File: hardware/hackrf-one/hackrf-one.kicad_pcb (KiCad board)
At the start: 4 copper layers, 120 x 75 mm, 444 parts, among them J1 USB-MICRO-B, J10 GND_CLIP, J2 RF-SHIELD-FRAME, J3 RF-SHIELD-COVER, J4 MOUNTING_HOLE, J5 MOUNTING_HOLE, J6 MOUNTING_HOLE, J7 MOUNTING_HOLE, J8 MOUNTING_HOLE, J9 MOUNTING_HOLE, P1 1V8, P13 GPO1, P14 XCVR_CLKOUT, P15 INTR, P16 CLKIN, P17 GPO6, P18 OEB, P19 GPO3, P2 CLKOUT, P20 GPIO, P21 REF_IN, P22 I2S, P23 DBGEN, P24 TRST, P25 LPC_ISP, P26 LPC_JTAG, P27 MIXER_SDATA, P28 SD, P29 CPLD_JTAG, P3 GND, P30 BANK2_AUX, P31 MIXER_SCLK, P32 MIXER_ENX, P33 MIXER_RESETX, P34 MIX_BYPASS, P35 !MIX_BYPASS, P36 VAA, P37 SCL, P38 SDA, P39 SSP1_SCK, P4 ANTENNA, P40 SSP1_MOSI, P41 SSP1_MISO, P42 TX, P43 RX, P44 HP, P45 LP, P46 TX_MIX_BP, P47 RX_MIX_BP, P48 TX_AMP, P49 RX_AMP, P5 LEDS, P50 AMP_BYPASS, P51 !TX_AMP_PWR, P52 !RX_AMP_PWR, P53 CS_XCVR, P54 CS_AD, P55 TXENABLE, P56 RXENABLE, P57 XTAL2, P58 GCK1, P59 GCK2, P6 GPO4, P60 SGPIO_CLK, P61 DA0, P62 DA7, P63 DD0, P64 DD9, P65 DA4, P66 DD5, P67 RSSI, P68 SPIFI_CS, P69 VREGMODE, P7 GPO2, P70 EN_1V8, P71 ID, P72 GP_CLKIN, P73 P1_2, P74 P1_1, P75 GP_CLKIN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

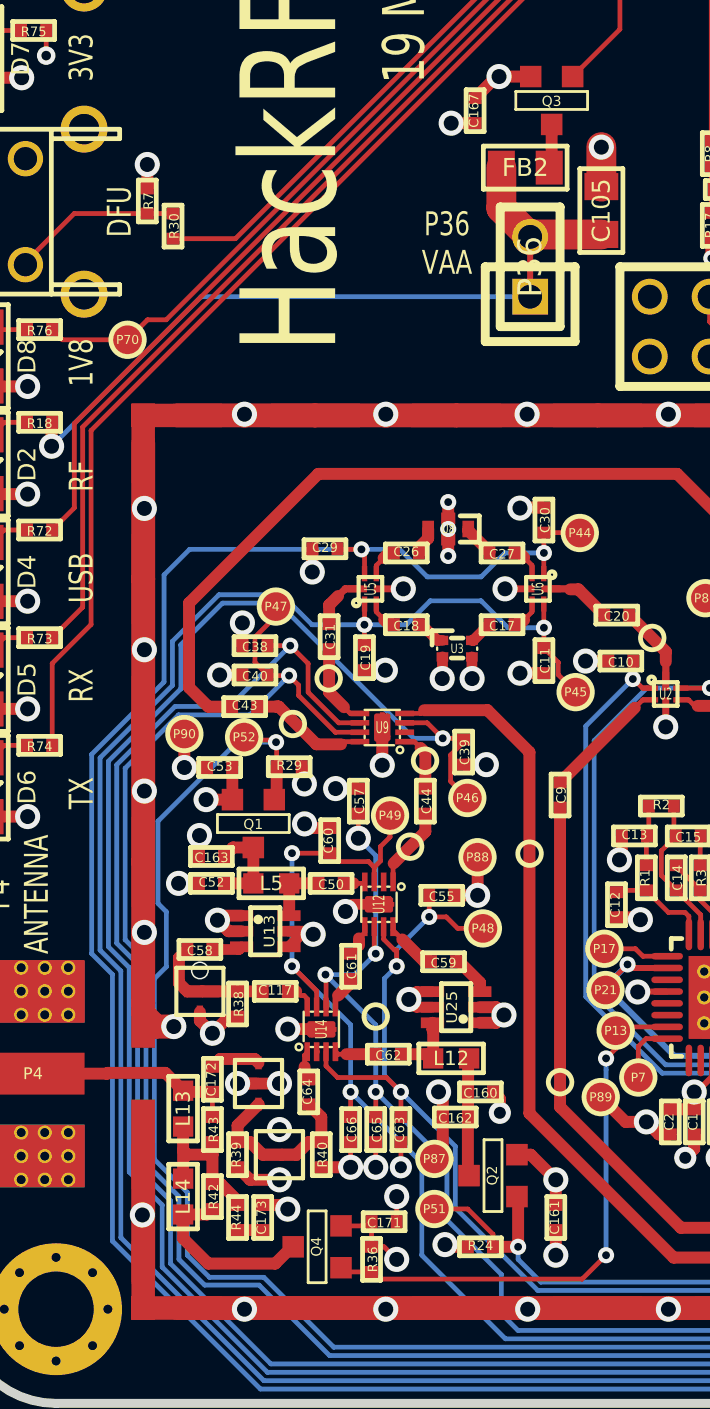
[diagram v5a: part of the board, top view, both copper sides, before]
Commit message: Updated U13 and U25 Rx and Tx amps from MGA-81563 to TRF37B73
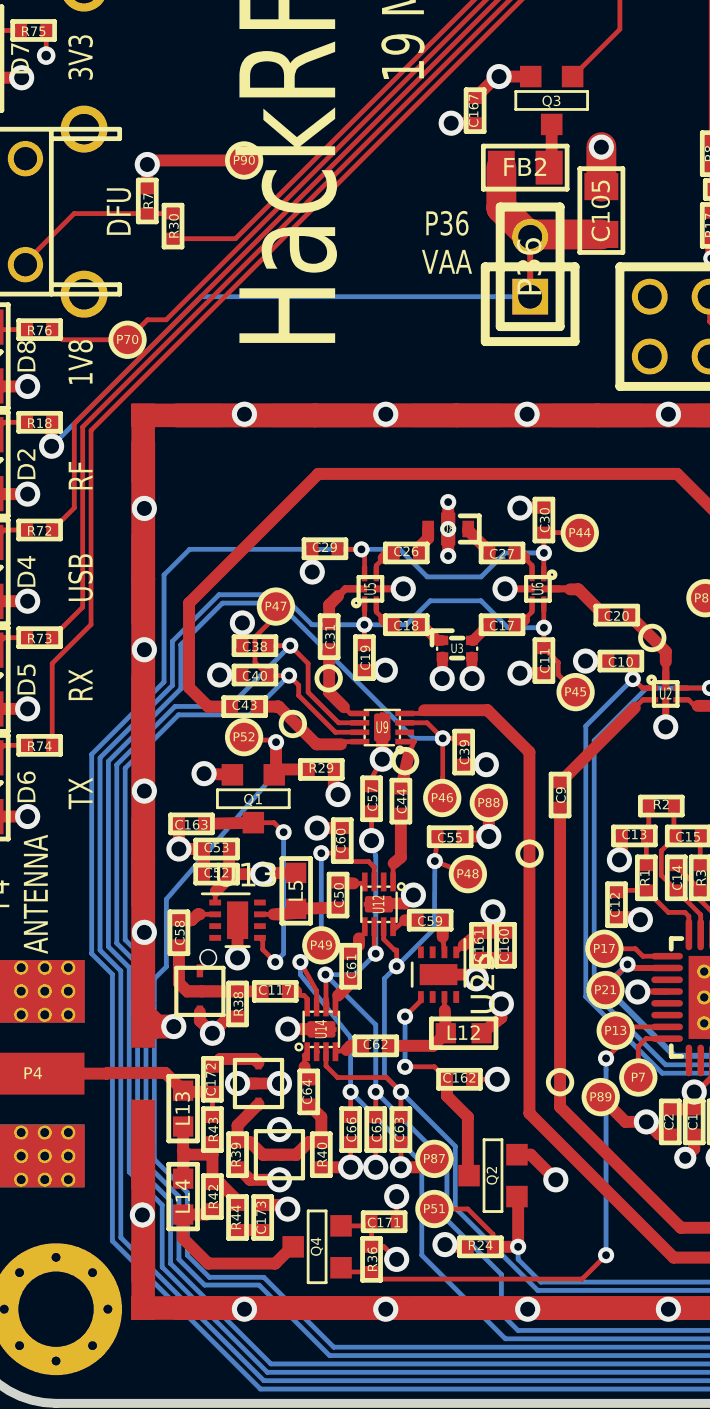
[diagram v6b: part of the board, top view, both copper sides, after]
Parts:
- removed the TESTPOINT-30MIL-MASKONLY at (77.6, 158.6)
- removed the TESTPOINT-30MIL-MASKONLY at (79.0, 151.4)
- U13, U25: value MGA-81563 -> TRF37B73; footprint hackrf:GSG-SOT363 -> Package_SON:WSON-8-1EP_2x2mm_P0.5mm_EP0.9x1.6mm
- moved P90 24.5 mm to (72.0, 122.2)
- moved C161 12.0 mm to (82.0, 155.6)
- moved C160 6.31 mm to (83.1, 155.6), turned to 270 degrees
- moved P49 6.24 mm to (75.3, 155.6)
- moved C53 3.46 mm to (70.8, 151.5)
- moved C55 2.51 mm to (80.7, 150.9)
- moved P48 2.39 mm to (81.5, 152.5)
- moved P88 2.35 mm to (82.4, 149.5)
- moved C59 1.85 mm to (79.9, 154.5)
- moved C163 1.62 mm to (69.8, 150.4)
- moved C162 1.61 mm to (81.1, 161.2), turned to 180 degrees
- moved U25 1.57 mm to (80.2, 156.8), turned to 270 degrees
- moved R29 1.37 mm to (75.3, 148.1)
- moved U13 1.27 mm to (71.7, 154.5), turned to 0 degrees
- moved L12 1.19 mm to (81.3, 159.3)
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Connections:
- C105 pad 1: Net-(C105-Pad1) -> VAA
- C125 pad 1: /mcu/usb/power/REG_OUT2 -> +1.8V
- C126 pad 1: /mcu/usb/power/REG_OUT2 -> +1.8V
- C127 pad 1: /mcu/usb/power/REG_OUT2 -> +1.8V
- C145 pad 2: /mcu/usb/power/REG_OUT1 -> VCC
- C146 pad 2: /mcu/usb/power/REG_OUT1 -> VCC
- C160 pad 1: Net-(C160-Pad1) -> VAA
- C162 pad 2: Net-(C160-Pad1) -> Net-(C162-Pad2)
- C50 pad 1: Net-(C50-Pad1) -> /frontend/RX_AMP_OUT
- C50 pad 2: /frontend/RX_AMP_OUT -> Net-(C50-Pad2)
- C52 pad 1: Net-(C163-Pad2) -> VAA
- C62 pad 1: /frontend/TX_AMP_OUT -> Net-(C62-Pad1)
- C62 pad 2: Net-(C62-Pad2) -> /frontend/TX_AMP_OUT
- FB2 pad 2: Net-(C105-Pad1) -> VAA
- L10 pad 2: /mcu/usb/power/REG_OUT2 -> +1.8V
- L11 pad 1: /mcu/usb/power/REG_OUT1 -> VCC
- L12 pad 1: Net-(C160-Pad1) -> VAA
- L12 pad 2: Net-(C62-Pad2) -> Net-(C62-Pad1)
- L5 pad 1: Net-(C163-Pad2) -> VAA
- L5 pad 2: Net-(C50-Pad1) -> /frontend/RX_AMP_OUT
- P1 pad 2: /mcu/usb/power/REG_OUT2 -> +1.8V
- P36 pad 2: Net-(C105-Pad1) -> VAA
- P8 pad 2: /mcu/usb/power/REG_OUT1 -> VCC
- Q2 pad D: Net-(C160-Pad1) -> Net-(C162-Pad2)
- R47 pad 1: /mcu/usb/power/REG_OUT2 -> +1.8V
- R56 pad 1: /mcu/usb/power/REG_OUT1 -> VCC
- U12 pad 4: /frontend/RX_AMP_OUT -> Net-(C50-Pad2)
- U13 pad 1: GND -> VAA
- U13 pad 2: GND -> Net-(C58-Pad2)
- U13 pad 3: Net-(C58-Pad2) -> Net-(U13-Pad3)
- U13 pad 4: GND -> Net-(U13-Pad4)
- U13 pad 5: GND -> Net-(C163-Pad2)
- U13 pad 6: Net-(C50-Pad1) -> Net-(U13-Pad6)
- U21 pad 4: /mcu/usb/power/REG_OUT1 -> VCC
- U25 pad 1: GND -> VAA
- U25 pad 2: GND -> Net-(C59-Pad2)
- U25 pad 3: Net-(C59-Pad2) -> Net-(U25-Pad3)
- U25 pad 4: GND -> Net-(U25-Pad4)
- U25 pad 5: GND -> Net-(C162-Pad2)
- U25 pad 6: Net-(C62-Pad2) -> Net-(U25-Pad6)
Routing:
- net +1.8V: track 49.8 -> 84.2 mm
- net /mcu/usb/power/REG_OUT2: track 34.4 -> 0.00 mm
- net /mcu/usb/power/REG_OUT1: track 34.3 -> 0.00 mm, vias 2 -> 0
- net VCC: track 183.7 -> 218.0 mm, vias 44 -> 46
- net VAA: track 95.1 -> 113.2 mm, vias 29 -> 32
- net Net-(C162-Pad2): track 0.00 -> 9.72 mm, vias 0 -> 2
- net Net-(C105-Pad1): track 9.05 -> 0.00 mm
- net Net-(C163-Pad2): track 4.17 -> 10.5 mm, vias 0 -> 2
- net Net-(C160-Pad1): track 5.35 -> 0.00 mm
- net Net-(C62-Pad1): track 0.00 -> 4.18 mm
- net Net-(C62-Pad2): track 2.98 -> 0.00 mm
- net /frontend/RX_AMP_OUT: track 0.90 -> 3.68 mm
- net Net-(C50-Pad1): track 2.62 -> 0.00 mm
- net RX_AMP: track 120.4 -> 117.9 mm
- net GND: track 593.3 -> 591.1 mm, vias 234 -> 227
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
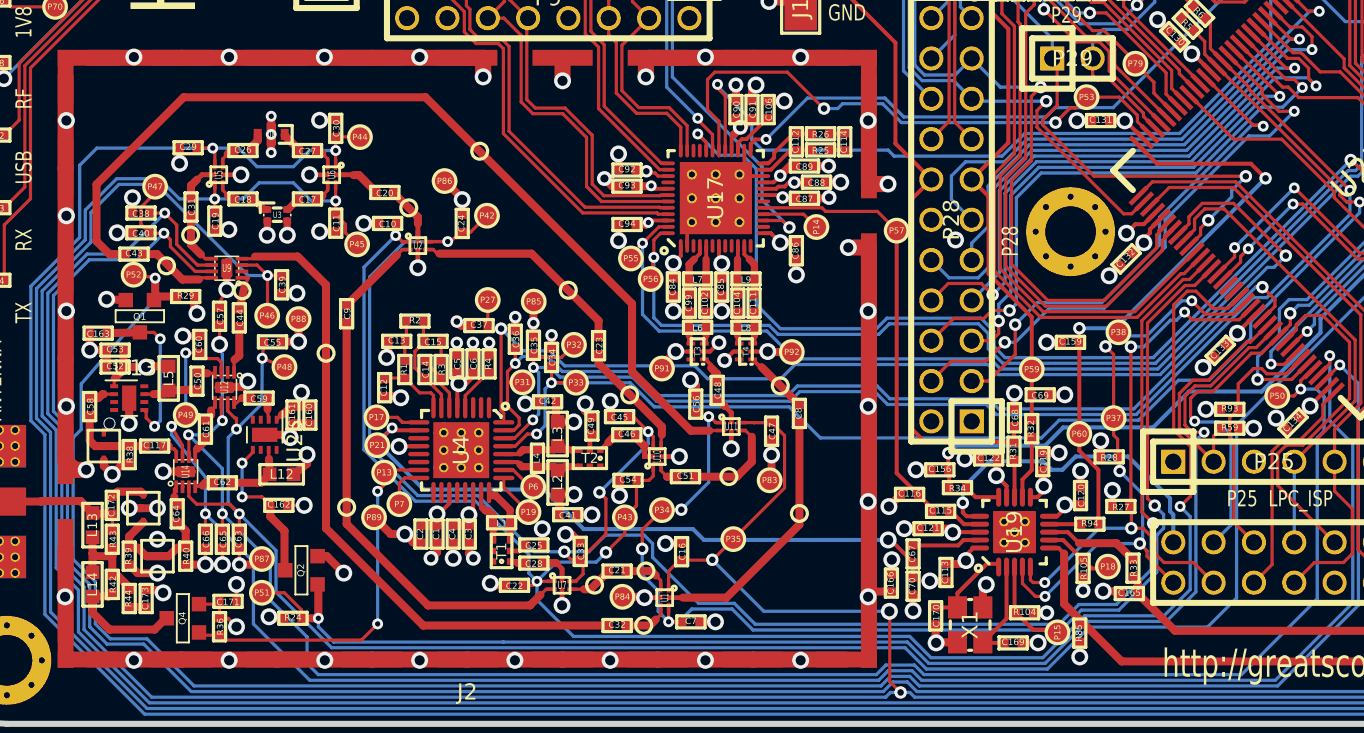
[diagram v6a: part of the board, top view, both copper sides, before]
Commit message: Updated U1, 2, 5, 6, 10, 11 from SKY13350 to SKY13453
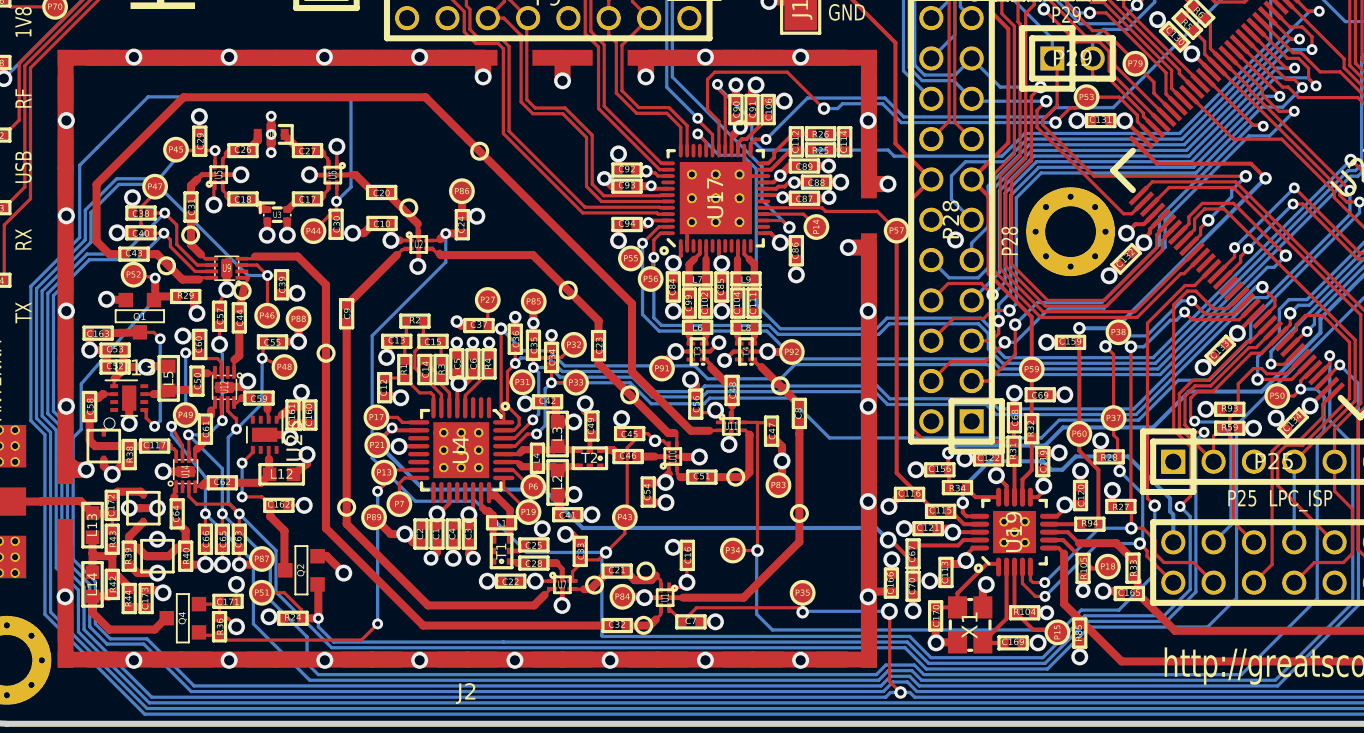
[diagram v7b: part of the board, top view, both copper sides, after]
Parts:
- removed C11, C19: 33pF, hackrf:GSG-0402
- removed P42: TX, hackrf:GSG-TESTPOINT-50MIL
- U1, U10, U11, U2, U5, U6, U7: value SKY13350 -> SKY13453; footprint hackrf:GSG-SKY13350-385LF -> gsg-modules:SKY13453-385LF
- moved P45 12.9 mm to (74.7, 138.8)
- moved P44 6.61 mm to (83.3, 144.0)
- moved C30 6.04 mm to (84.7, 143.5)
- moved P35 5.52 mm to (114.1, 166.8)
- moved P34 5.14 mm to (109.7, 164.1)
- moved C54 1.47 mm to (104.4, 160.4), turned to 270 degrees
- moved C46 1.37 mm to (103.1, 158.2)
- moved P86 1.26 mm to (92.7, 141.5)
- moved C45 1.24 mm to (103.2, 156.7)
- moved C51 1.03 mm to (107.8, 159.5)
- moved U10 0.98 mm to (105.9, 158.2)
- moved C48 0.94 mm to (109.7, 154.0)
- moved C29 0.84 mm to (76.2, 138.3), turned to 90 degrees
- moved P83 0.64 mm to (112.6, 160.0)
- moved TESTPOINT-30MIL-MASKONLY 0.43 mm to (109.9, 159.5)
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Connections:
- C10 pad 2: RX -> VAA
- C16 pad 1: !MIX_BYPASS -> VAA
- C22 pad 2: RX -> VAA
- C24 pad 2: TX -> RX
- C29 pad 1: HP -> LP
- C30 pad 1: HP -> GND
- C30 pad 2: GND -> HP
- C33 pad 1: TX -> RX
- C45 pad 2: TX -> RX
- C47 pad 2: !MIX_BYPASS -> MIX_BYPASS
- C54 pad 1: RX -> VAA
- C56 pad 1: MIX_BYPASS -> VAA
- C7 pad 2: MIX_BYPASS -> !MIX_BYPASS
- U1 pad 1: !MIX_BYPASS -> VAA
- U1 pad 5: MIX_BYPASS -> !MIX_BYPASS
- U10 pad 1: RX -> VAA
- U10 pad 5: TX -> RX
- U11 pad 1: MIX_BYPASS -> VAA
- U11 pad 5: !MIX_BYPASS -> MIX_BYPASS
- U2 pad 1: RX -> VAA
- U2 pad 5: TX -> RX
- U5 pad 1: LP -> VAA
- U5 pad 5: HP -> LP
- U6 pad 1: HP -> VAA
- U6 pad 5: LP -> HP
- U7 pad 1: RX -> VAA
- U7 pad 5: TX -> RX
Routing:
- net TX: track 115.0 -> 0.00 mm, vias 5 -> 0
- net VAA: track 113.2 -> 126.8 mm, vias 32 -> 39
- net !MIX_BYPASS: track 237.4 -> 224.0 mm
- net LP: track 225.5 -> 214.4 mm, vias 3 -> 2
- net MIX_BYPASS: track 74.6 -> 64.0 mm, vias 5 -> 2
- net HP: track 202.5 -> 209.1 mm, vias 3 -> 2
- net RX: track 114.9 -> 118.4 mm
- net GND: track 591.1 -> 590.1 mm, vias 227 -> 224
- net Net-(C23-Pad1): track 7.48 -> 8.18 mm
- net RX_IF: track 1.80 -> 2.44 mm
- net Net-(C51-Pad1): track 6.42 -> 5.79 mm
- net Net-(C8-Pad2): track 16.4 -> 17.1 mm
